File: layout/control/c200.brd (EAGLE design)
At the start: 200 x 50 mm, 71 parts, among them IC1 STM32F103C8T, IC2 LP2985-SOT23-5, IC3 IC_USBLC6-2, IC4 IC_USBLC6-2, IC5 LT1619ES8, IC6 LP2985-SOT23-5, IC7 IRF7470, T1 LPISR, Y1 532-CRYSTAL, Y2 EQ161-CRYSTAL

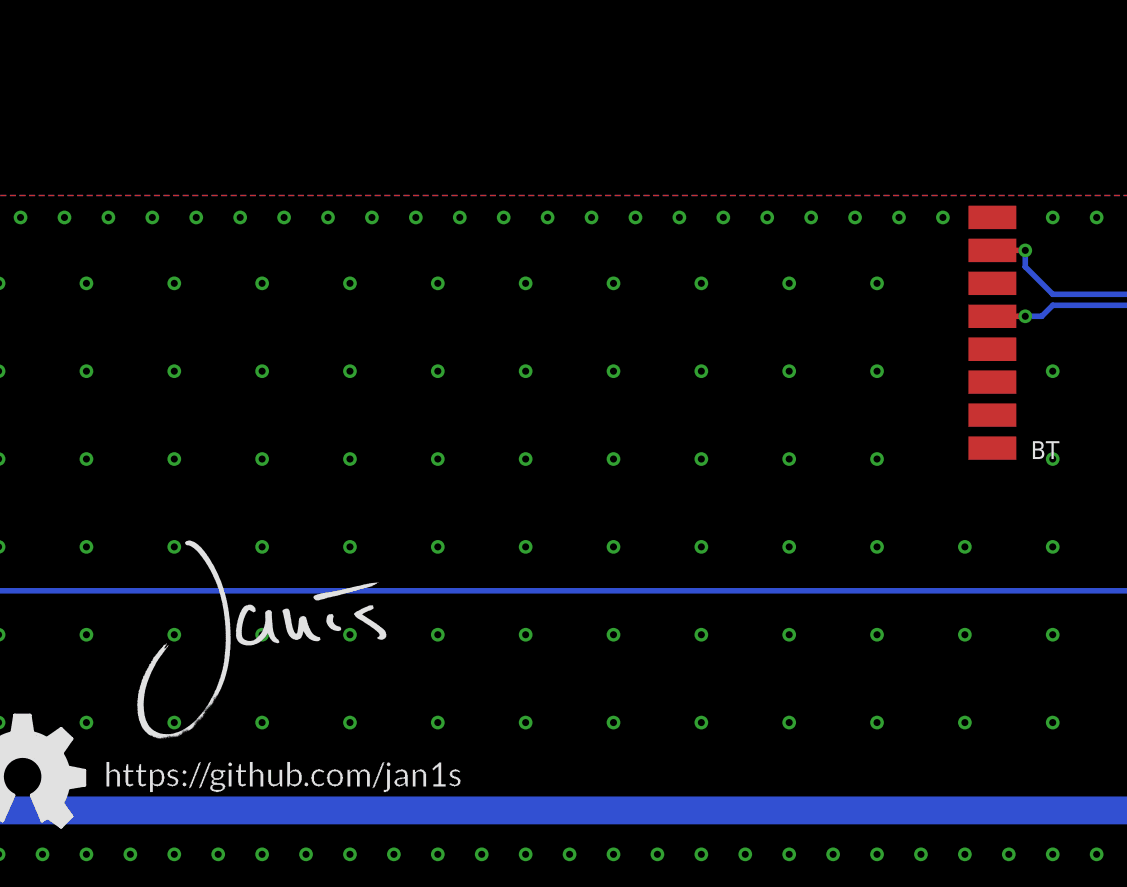
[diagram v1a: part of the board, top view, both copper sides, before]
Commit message: Added ESP-12
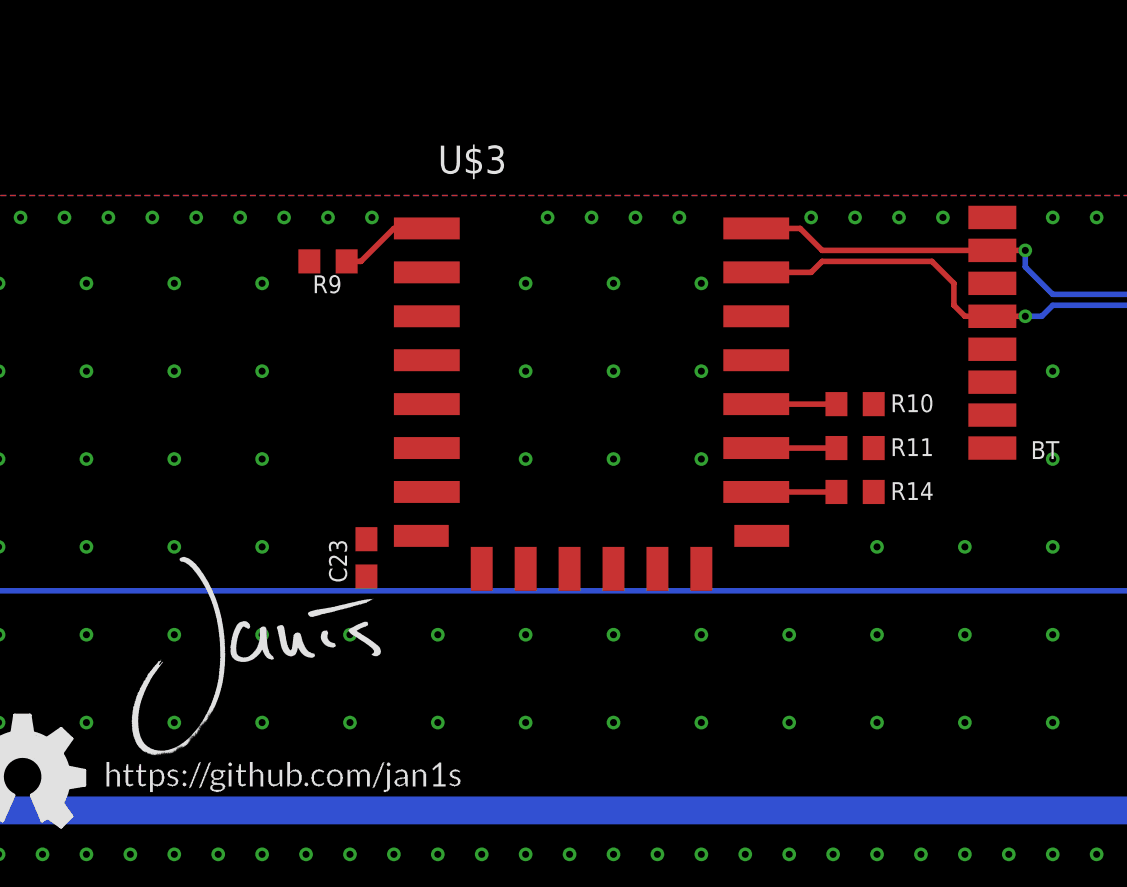
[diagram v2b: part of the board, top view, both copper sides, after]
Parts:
- added C23: 1µF, rcl:C0603
- added R10, R11, R14, R9: 10k, rcl:R0603
- added U$3: ESP-12F, espressif:ESP-12F
- moved U$1 0.79 mm to (93.8, 6.25)
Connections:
- removed net BT_USER: BT.16, IC1.11, R8.2
- removed net N$32: IC1.19
- removed net N$34: IC1.20
- removed net N$42: IC1.10
- new net N$6: R14.1, U$3.16
- new net RFMOD_DBG: IC1.19, R11.1, U$3.17
- new net RFMOD_EN: BT.16, IC1.11, R8.2, U$3.3
- new net RFMOD_FLASH: IC1.20, R10.1, U$3.18
- new net RFMOD_RST: BT.11, IC1.10, R9.1, U$3.1
- net +3V3: now also C23.1, R10.2, R11.2, R9.2, U$3.8
- net GND: now also C23.2, R14.2, U$3.15
- net USART2_RX: now also U$3.22
- net USART2_TX: now also U$3.21
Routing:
- net RFMOD_EN: track 0.00 -> 38.1 mm
- net BT_USER: track 38.1 -> 0.00 mm
- net USART2_TX: track 48.3 -> 60.9 mm
- net USART2_RX: track 47.7 -> 58.8 mm
- net RFMOD_RST: track 0.00 -> 4.27 mm
- net RFMOD_FLASH: track 0.00 -> 3.65 mm
- net RFMOD_DBG: track 0.00 -> 3.65 mm
- net N$6: track 0.00 -> 3.65 mm
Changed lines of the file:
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@@
 <?xml version="1.0" encoding="utf-8"?>
 <!DOCTYPE eagle SYSTEM "eagle.dtd">
-<eagle version="6.1">
+<eagle version="7.6.0">
 <drawing>
 <settings>
@@
 <layer number="54" name="bGND_GNDA" color="1" fill="9" visible="no" active="no"/>
 <layer number="56" name="wert" color="7" fill="1" visible="yes" active="yes"/>
+<layer number="90" name="Modules" color="5" fill="1" visible="no" active="no"/>
 <layer number="91" name="Nets" color="2" fill="1" visible="no" active="no"/>
 <layer number="92" name="Busses" color="1" fill="1" visible="no" active="no"/>
@@
 </class>
 </classes>
-<designrules>
+<designrules name="default">
 <description language="de">&lt;b&gt;EAGLE Design Rules&lt;/b&gt;
 &lt;p&gt;
@@
 <pass name="Default">
 <param name="RoutingGrid" value="50mil"/>
+<param name="AutoGrid" value="1"/>
+<param name="Efforts" value="0"/>
+<param name="TopRouterVariant" value="1"/>
 <param name="tpViaShape" value="round"/>
 <param name="PrefDir.1" value="|"/>
@@
 <attribute name="NAME" x="187.135" y="19.385" size="0.8128" layer="25" rot="R270"/>
 </element>
-<element name="U$1" library="pcb-artwork" package="JANIS_10MM" value="" x="94" y="7"/>
+<element name="U$1" library="pcb-artwork" package="JANIS_10MM" value="" x="93.75" y="6.25"/>
 <element name="R6" library="rcl" package="R0603" value="1k5" x="185.75" y="11.75" smashed="yes" rot="R270">
 <attribute name="NAME" x="189.615" y="9.615" size="0.8128" layer="25" rot="R90"/>
@@
 </element>
 <element name="LOGO2" library="ohw-logo" package="OSHW_FILLX200_NOTEXT" value="OSHW_LOGO_FILLX0200-NT" x="86.25" y="3.25"/>
+<element name="U$3" library="espressif" package="ESP-12F" value="ESP-12F" x="115" y="39"/>
+<element name="C23" library="rcl" package="C0603" value="1µF" x="104.75" y="15.5" smashed="yes" rot="R270">
+<attribute name="NAME" x="103.865" y="14.365" size="0.8128" layer="25" rot="R90"/>
+</element>
+<element name="R9" library="rcl" package="R0603" value="10k" x="103" y="29" smashed="yes" rot="R180">
+<attribute name="NAME" x="103.635" y="28.365" size="0.8128" layer="25" rot="R180"/>
+</element>
+<element name="R10" library="rcl" package="R0603" value="10k" x="127" y="22.5" smashed="yes">
+<attribute name="NAME" x="128.615" y="22.135" size="0.8128" layer="25"/>
+</element>
+<element name="R11" library="rcl" package="R0603" value="10k" x="127" y="20.5" smashed="yes">
+<attribute name="NAME" x="128.615" y="20.135" size="0.8128" layer="25"/>
+</element>
+<element name="R14" library="rcl" package="R0603" value="10k" x="127" y="18.5" smashed="yes">
+<attribute name="NAME" x="128.615" y="18.135" size="0.8128" layer="25"/>
+</element>
 </elements>
 <signals>
@@
 <via x="103" y="31" extent="1-16" drill="0.32"/>
 <via x="105" y="31" extent="1-16" drill="0.32"/>
-<via x="107" y="31" extent="1-16" drill="0.32"/>
-<via x="109" y="31" extent="1-16" drill="0.32"/>
-<via x="111" y="31" extent="1-16" drill="0.32"/>
 <via x="113" y="31" extent="1-16" drill="0.32"/>
 <via x="115" y="31" extent="1-16" drill="0.32"/>
 <via x="117" y="31" extent="1-16" drill="0.32"/>
 <via x="119" y="31" extent="1-16" drill="0.32"/>
-<via x="121" y="31" extent="1-16" drill="0.32"/>
-<via x="123" y="31" extent="1-16" drill="0.32"/>
 <via x="125" y="31" extent="1-16" drill="0.32"/>
 <via x="127" y="31" extent="1-16" drill="0.32"/>
@@
 <via x="96" y="28" extent="1-16" drill="0.32"/>
 <via x="100" y="28" extent="1-16" drill="0.32"/>
-<via x="104" y="16" extent="1-16" drill="0.32"/>
-<via x="104" y="20" extent="1-16" drill="0.32"/>
-<via x="104" y="24" extent="1-16" drill="0.32"/>
-<via x="104" y="28" extent="1-16" drill="0.32"/>
-<via x="108" y="28" extent="1-16" drill="0.32"/>
-<via x="108" y="24" extent="1-16" drill="0.32"/>
-<via x="108" y="20" extent="1-16" drill="0.32"/>
-<via x="108" y="16" extent="1-16" drill="0.32"/>
-<via x="112" y="16" extent="1-16" drill="0.32"/>
 <via x="112" y="20" extent="1-16" drill="0.32"/>
 <via x="112" y="24" extent="1-16" drill="0.32"/>
@@
 <via x="116" y="24" extent="1-16" drill="0.32"/>
 <via x="116" y="20" extent="1-16" drill="0.32"/>
-<via x="116" y="16" extent="1-16" drill="0.32"/>
-<via x="120" y="16" extent="1-16" drill="0.32"/>
 <via x="120" y="20" extent="1-16" drill="0.32"/>
 <via x="120" y="24" extent="1-16" drill="0.32"/>
 <via x="120" y="28" extent="1-16" drill="0.32"/>
-<via x="124" y="28" extent="1-16" drill="0.32"/>
-<via x="124" y="24" extent="1-16" drill="0.32"/>
-<via x="124" y="20" extent="1-16" drill="0.32"/>
-<via x="124" y="16" extent="1-16" drill="0.32"/>
 <via x="128" y="16" extent="1-16" drill="0.32"/>
-<via x="128" y="20" extent="1-16" drill="0.32"/>
-<via x="128" y="24" extent="1-16" drill="0.32"/>
-<via x="128" y="28" extent="1-16" drill="0.32"/>
+<contactref element="U$3" pad="15"/>
+<contactref element="C23" pad="2"/>
+<contactref element="R14" pad="2"/>
 </signal>
 <signal name="+5V">
@@
 <wire x1="150.85" y1="29.65" x2="152" y2="28.5" width="0.254" layer="1"/>
 <wire x1="152" y1="28" x2="152" y2="28.5" width="0.254" layer="1"/>
+<contactref element="U$3" pad="8"/>
+<contactref element="C23" pad="1"/>
+<contactref element="R10" pad="2"/>
+<contactref element="R11" pad="2"/>
+<contactref element="R9" pad="2"/>
+<wire x1="127.85" y1="20.5" x2="146.75" y2="20.5" width="0" layer="19" extent="1-1"/>
+<wire x1="127.85" y1="22.5" x2="127.85" y2="20.5" width="0" layer="19" extent="1-1"/>
+<wire x1="107.25" y1="16.5" x2="127.85" y2="20.5" width="0" layer="19" extent="1-1"/>
+<wire x1="104.75" y1="16.35" x2="107.25" y2="16.5" width="0" layer="19" extent="1-1"/>
+<wire x1="102.15" y1="29" x2="104.75" y2="16.35" width="0" layer="19" extent="1-1"/>
 </signal>
 <signal name="N$20">
@@
 <wire x1="134.75" y1="26.5" x2="135.5" y2="26.5" width="0.254" layer="16"/>
 <wire x1="135.5" y1="26.5" x2="136" y2="27" width="0.254" layer="16"/>
+<contactref element="U$3" pad="21"/>
+<wire x1="133.25" y1="26.5" x2="132" y2="26.5" width="0.254" layer="1"/>
+<wire x1="132" y1="26.5" x2="131.5" y2="27" width="0.254" layer="1"/>
+<wire x1="131.5" y1="27" x2="131.5" y2="28" width="0.254" layer="1"/>
+<wire x1="122.5" y1="28.5" x2="125" y2="28.5" width="0.254" layer="1"/>
+<wire x1="125" y1="28.5" x2="125.5" y2="29" width="0.254" layer="1"/>
+<wire x1="125.5" y1="29" x2="130.5" y2="29" width="0.254" layer="1"/>
+<wire x1="130.5" y1="29" x2="131.5" y2="28" width="0.254" layer="1"/>
 </signal>
 <signal name="USART2_RX">
@@
 <wire x1="136" y1="27.5" x2="134.75" y2="28.75" width="0.254" layer="16"/>
 <wire x1="134.75" y1="28.75" x2="134.75" y2="29.5" width="0.254" layer="16"/>
+<contactref element="U$3" pad="22"/>
+<wire x1="133.25" y1="29.5" x2="125.5" y2="29.5" width="0.254" layer="1"/>
+<wire x1="122.5" y1="30.5" x2="124.5" y2="30.5" width="0.254" layer="1"/>
+<wire x1="124.5" y1="30.5" x2="125.5" y2="29.5" width="0.254" layer="1"/>
 </signal>
 <signal name="SPI1_SCK">
@@
 <wire x1="175.05" y1="18.55" x2="176.55" y2="18.55" width="0.254" layer="1"/>
 </signal>
-<signal name="N$42">
-<contactref element="IC1" pad="10"/>
-</signal>
 <signal name="SWDIO">
 <contactref element="IC1" pad="34"/>
@@
 <contactref element="IC1" pad="38"/>
 </signal>
-<signal name="N$32">
+<signal name="RFMOD_DBG">
 <contactref element="IC1" pad="19"/>
-</signal>
-<signal name="N$34">
-<contactref element="IC1" pad="20"/>
+<contactref element="U$3" pad="17"/>
+<contactref element="R11" pad="1"/>
+<wire x1="122.5" y1="20.5" x2="126.15" y2="20.5" width="0.254" layer="1"/>
+<wire x1="126.15" y1="20.5" x2="177.75" y2="26.75" width="0" layer="19" extent="1-1"/>
 </signal>
 <signal name="JTDO">
@@
 <wire x1="150.4" y1="26.4" x2="150.5" y2="26.5" width="0.254" layer="1"/>
 </signal>
-<signal name="BT_USER">
+<signal name="RFMOD_EN">
 <contactref element="BT" pad="16"/>
 <contactref element="R8" pad="2"/>
@@
 <wire x1="146.75" y1="31" x2="148.9" y2="31" width="0.254" layer="1"/>
 <wire x1="148.9" y1="31" x2="149" y2="31.35" width="0.254" layer="1"/>
+<contactref element="U$3" pad="3"/>
+<wire x1="107.5" y1="26.5" x2="146.75" y2="31" width="0" layer="19" extent="1-1"/>
+</signal>
+<signal name="RFMOD_RST">
+<contactref element="U$3" pad="1"/>
+<contactref element="BT" pad="11"/>
+<contactref element="R9" pad="1"/>
+<contactref element="IC1" pad="10"/>
+<wire x1="103.85" y1="29" x2="104.5" y2="29" width="0.254" layer="1"/>
+<wire x1="104.5" y1="29" x2="106" y2="30.5" width="0.254" layer="1"/>
+<wire x1="107.5" y1="30.5" x2="106" y2="30.5" width="0.254" layer="1"/>
+<wire x1="146.75" y1="23.5" x2="180.25" y2="31.25" width="0" layer="19" extent="1-1"/>
+<wire x1="107.5" y1="30.5" x2="146.75" y2="23.5" width="0" layer="19" extent="1-1"/>
+</signal>
+<signal name="RFMOD_FLASH">
+<contactref element="U$3" pad="18"/>
+<contactref element="R10" pad="1"/>
+<contactref element="IC1" pad="20"/>
+<wire x1="122.5" y1="22.5" x2="126.15" y2="22.5" width="0.254" layer="1"/>
+<wire x1="126.15" y1="22.5" x2="177.75" y2="26.25" width="0" layer="19" extent="1-1"/>
+</signal>
+<signal name="N$6">
+<contactref element="U$3" pad="16"/>
+<contactref element="R14" pad="1"/>
+<wire x1="122.5" y1="18.5" x2="126.15" y2="18.5" width="0.254" layer="1"/>
 </signal>
 </signals>
